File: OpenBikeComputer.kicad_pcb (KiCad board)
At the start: 4 copper layers, 80 x 80 mm, 53 parts, among them J1 USB_C_Receptacle_USB2.0_14P, J2 RJ45_Shielded, J4 Micro_SD_Card_Det1, J5 Conn_01x24_Socket, J6 Conn_01x03_Pin, J7 RFShield_TwoPieces, J8 Conn_01x02_Socket, U1 nRF54L15-QFXX, U2 nPM1300-QEXX, U3 BQ298012RUGR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

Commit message: begin new board
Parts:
- removed J5: Conn_01x24_Socket, Connector_FFC-FPC:TE_2-84952-4_1x24-1MP_P1.0mm_Horizontal
- added J3: Conn_01x30_Socket, Library:CON_541043031_MOL, B.Cu at (172.5, 98.1)
- added SW1: SW_Push, Button_Switch_SMD:SW_SPST_PTS647_Sx50, F.Cu at (157.5, 121.0)
- added SW2: SW_Push, Button_Switch_SMD:SW_SPST_PTS647_Sx50, F.Cu at (167.5, 121.0)
- added SW3: SW_Push, Button_Switch_SMD:SW_SPST_PTS647_Sx50, F.Cu at (177.5, 121.0)
- added SW4: SW_Push, Button_Switch_SMD:SW_SPST_PTS647_Sx50, F.Cu at (187.5, 121.0)
- J1: moved to B.Cu
- J2, J6, R7, R8: moved to F.Cu
- moved J8 67.3 mm to (156.9, 81.5), turned to 90 degrees
- moved U8 66.3 mm to (243.6, 128.9)
- moved D2 61.5 mm to (249.8, 122.8)
- moved L2 61.0 mm to (254.6, 126.8), turned to 0 degrees
- moved R2 61.0 mm to (240.4, 130.2), turned to 0 degrees
- moved D3 60.8 mm to (249.8, 125.8)
- moved D4 60.6 mm to (249.8, 128.9)
- moved C7 60.1 mm to (243.3, 126.2), turned to 0 degrees
- moved R1 59.8 mm to (240.4, 128.2), turned to 0 degrees
- moved C1 59.6 mm to (240.4, 122.3)
- moved C2 58.2 mm to (240.4, 124.2), turned to 0 degrees
- moved C3 57.2 mm to (240.4, 126.2), turned to 0 degrees
- moved U2 57.1 mm to (254.3, 114.9), turned to 0 degrees
- moved L1 56.1 mm to (254.6, 123.1), turned to 0 degrees
- moved C9 55.6 mm to (246.1, 124.2), turned to 0 degrees
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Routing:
- net VDDIO: track 150.7 -> 0.00 mm, vias 9 -> 0
- net SENSE2A: track 54.9 -> 0.00 mm, vias 1 -> 0
- net DETECT1: track 52.8 -> 0.00 mm, vias 1 -> 0
- net SENSE1A: track 52.7 -> 0.00 mm, vias 1 -> 0
- net Net-(J6-Pin_2): track 49.3 -> 0.00 mm, vias 1 -> 0
- net SENSE2B: track 49.3 -> 0.00 mm, vias 1 -> 0
- net Net-(J6-Pin_3): track 48.8 -> 0.00 mm, vias 1 -> 0
- net DETECT2: track 48.6 -> 0.00 mm, vias 1 -> 0
- net SENSE1B: track 47.7 -> 0.00 mm, vias 1 -> 0
- net Net-(AE2-A): track 33.7 -> 0.00 mm
- net SCL1: track 33.1 -> 0.00 mm, vias 2 -> 0
- net VSYS: track 32.3 -> 0.00 mm
- net SDA1: track 31.5 -> 0.00 mm, vias 2 -> 0
- net SD_CS: track 24.1 -> 0.00 mm, vias 2 -> 0
- net SD_MISO: track 24.1 -> 0.00 mm, vias 2 -> 0
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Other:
- board size 80 x 80 mm -> 45 x 60 mm

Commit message: lay out components
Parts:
- removed J2: RJ45_Shielded, Connector_RJ:RJ45_Amphenol_RJHSE538X
- added REF**: NHD-1.91-176176UBC3, Library:NHD-1.91-176176UBC3, F.Cu at (163.2, 85.8)
- J4: moved to B.Cu
- moved J4 87.6 mm to (156.2, 94.4), turned to 90 degrees
- moved J7 50.9 mm to (175.6, 98.7)
- moved AE2 47.1 mm to (189.2, 98.9), turned to -90 degrees
- moved J3 8.40 mm to (172.5, 106.5)
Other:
- outline, holes or cut-outs redrawn

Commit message: housekeeping
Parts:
- moved J6 110.8 mm to (151.6, 103.9)
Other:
- board text removed: "20250126_ly2_s6_w12"
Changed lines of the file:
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@@
 	(footprint "Connector_PinHeader_1.27mm:PinHeader_1x03_P1.27mm_Vertical"
 		(layer "F.Cu")
-		(at 261.5 89.53)
+		(at 151.6 103.86)
 		(descr "Through hole straight pin header, 1x03, 1.27mm pitch, single row")
 		(tags "Through hole pin header THT 1x03 1.27mm single row")
@@
 	)
 	(footprint "RF_Antenna:Texas_SWRA117D_2.4GHz_Right"
+		(locked yes)
 		(layer "F.Cu")
 		(at 189.175 98.9 -90)
@@
 	)
 	(footprint "Library:CON_541043031_MOL"
+		(locked yes)
 		(layer "B.Cu")
 		(at 172.5 106.5 180)
@@
 	)
 	(gr_line
-		(start 6.825 11.821246)
-		(end 20.25115 35.07602)
-		(stroke
-			(width 0.127)
-			(type default)
-		)
-		(layer "F.SilkS")
-	)
-	(gr_line
-		(start 13.65 0)
-		(end 40.5023 0)
-		(stroke
-			(width 0.127)
-			(type default)
-		)
-		(layer "F.SilkS")
-	)
-	(gr_line
-		(start -6.825 -11.821246)
-		(end -20.25115 -35.07602)
-		(stroke
-			(width 0.127)
-			(type default)
-		)
-		(layer "F.SilkS")
-	)
-	(gr_line
-		(start -13.65 0)
-		(end -40.5023 0)
-		(stroke
-			(width 0.127)
-			(type default)
-		)
-		(layer "F.SilkS")
-	)
-	(gr_line
-		(start -6.824999 11.821246)
-		(end -20.251149 35.07602)
-		(stroke
-			(width 0.127)
-			(type default)
-		)
-		(layer "F.SilkS")
-	)
-	(gr_circle
-		(center 0 0)
-		(end 13 0)
-		(stroke
-			(width 0.1)
-			(type default)
-		)
-		(fill none)
-		(layer "F.SilkS")
-	)
-	(gr_circle
-		(center 0 0)
-		(end 42.634 0)
-		(stroke
-			(width 0.1)
-			(type default)
-		)
-		(fill none)
-		(layer "F.SilkS")
-	)
-	(gr_line
-		(start 6.824999 -11.821246)
-		(end 20.251149 -35.07602)
-		(stroke
-			(width 0.127)
-			(type default)
-		)
-		(layer "F.SilkS")
-	)
-	(gr_line
 		(start 195 135)
 		(end 195 75)
@@
 		)
 	)
-	(gr_text "20250126_ly2_s6_w12"
-		(at 0 48.5 0)
-		(layer "F.SilkS")
-		(effects
-			(font
-				(size 0.5 0.5)
-			)
-		)
-	)
 	(zone
 		(net 0)
 		(net_name "")
+		(locked yes)
 		(layers "F.Cu" "In1.Cu" "In2.Cu" "B.Cu")
 		(name "antenna")
@@
 		(polygon
 			(pts
-				(xy 189.4 97.5) (xy 188.5 97.5) (xy 188.5 112.5) (xy 195 112.5) (xy 195 95) (xy 189.4 95)
+				(xy 189.4 99.5) (xy 188.5 99.5) (xy 188.5 112.5) (xy 195 112.5) (xy 195 95) (xy 189.4 95)
 			)
 		)
@@
 			)
 		)
-	)
-	(zone
-		(net 0)
-		(net_name "")
-		(layers "*.Mask")
-		(hatch edge 0.5)
-		(connect_pads
-			(clearance 0)
-		)
-		(min_thickness 0.25)
-		(filled_areas_thickness no)
-		(fill yes
-			(thermal_gap 0.5)
-			(thermal_bridge_width 0.5)
-			(island_removal_mode 1)
-			(island_area_min 10)
-		)
-		(polygon
-			(pts
-				(xy 49.999999 20.710678) (xy 20.710678 49.999999) (xy -20.710678 49.999999) (xy -49.999999 20.710678)
-				(xy -49.999999 -20.710678) (xy -20.710678 -49.999999) (xy 20.710678 -49.999999) (xy 49.999999 -20.710678)
-			)
-		)
-		(polygon
-			(pts
-				(xy 44.999999 18.63961) (xy 18.63961 44.999999) (xy -18.63961 44.999999) (xy -44.999999 18.63961)
-				(xy -44.999999 -18.63961) (xy -18.63961 -44.999999) (xy 18.63961 -44.999999) (xy 44.999999 -18.63961)
-			)
-		)
-	)
-	(zone
-		(net 0)
-		(net_name "")
-		(layers "*.Mask")
-		(hatch edge 0.5)
-		(connect_pads
-			(clearance 0)
-		)
-		(min_thickness 0.25)
-		(filled_areas_thickness no)
-		(fill yes
-			(thermal_gap 0.5)
-			(thermal_bridge_width 0.5)
-			(island_removal_mode 1)
-			(island_area_min 10)
-		)
-		(polygon
-			(pts
-				(xy 11.392 0) (xy 11.36952 0.715309) (xy 11.30217 1.427796) (xy 11.190216 2.134647) (xy 11.034099 2.833075)
-				(xy 10.834435 3.520321) (xy 10.592013 4.193674) (xy 10.307789 4.850477) (xy 9.982885 5.488137) (xy 9.618583 6.104138)
-				(xy 9.216321 6.696049) (xy 8.777686 7.261534) (xy 8.30441 7.79836) (xy 7.79836 8.30441) (xy 7.261534 8.777686)
-				(xy 6.696049 9.216321) (xy 6.104138 9.618583) (xy 5.488137 9.982885) (xy 4.850477 10.307789) (xy 4.193674 10.592013)
-				(xy 3.520321 10.834435) (xy 2.833075 11.034099) (xy 2.134647 11.190216) (xy 1.427796 11.30217) (xy 0.715309 11.36952)
-				(xy 0 11.392) (xy -0.715309 11.36952) (xy -1.427796 11.30217) (xy -2.134647 11.190216) (xy -2.833075 11.034099)
-				(xy -3.520321 10.834435) (xy -4.193674 10.592013) (xy -4.850477 10.307789) (xy -5.488137 9.982885)
-				(xy -6.104138 9.618583) (xy -6.696049 9.216321) (xy -7.261534 8.777686) (xy -7.79836 8.30441) (xy -8.30441 7.79836)
-				(xy -8.777686 7.261534) (xy -9.216321 6.696049) (xy -9.618583 6.104138) (xy -9.982885 5.488137)
-				(xy -10.307789 4.850477) (xy -10.592013 4.193674) (xy -10.834435 3.520321) (xy -11.034099 2.833075)
-				(xy -11.190216 2.134647) (xy -11.30217 1.427796) (xy -11.36952 0.715309) (xy -11.392 0) (xy -11.36952 -0.715309)
-				(xy -11.30217 -1.427796) (xy -11.190216 -2.134647) (xy -11.034099 -2.833075) (xy -10.834435 -3.520321)
-				(xy -10.592013 -4.193674) (xy -10.307789 -4.850477) (xy -9.982885 -5.488137) (xy -9.618583 -6.104138)
-				(xy -9.216321 -6.696049) (xy -8.777686 -7.261534) (xy -8.30441 -7.79836) (xy -7.79836 -8.30441)
-				(xy -7.261534 -8.777686) (xy -6.696049 -9.216321) (xy -6.104138 -9.618583) (xy -5.488137 -9.982885)
-				(xy -4.850477 -10.307789) (xy -4.193674 -10.592013) (xy -3.520321 -10.834435) (xy -2.833075 -11.034099)
-				(xy -2.134647 -11.190216) (xy -1.427796 -11.30217) (xy -0.715309 -11.36952) (xy 0 -11.392) (xy 0.715309 -11.36952)
-				(xy 1.427796 -11.30217) (xy 2.134647 -11.190216) (xy 2.833075 -11.034099) (xy 3.520321 -10.834435)
-				(xy 4.193674 -10.592013) (xy 4.850477 -10.307789) (xy 5.488137 -9.982885) (xy 6.104138 -9.618583)
-				(xy 6.696049 -9.216321) (xy 7.261534 -8.777686) (xy 7.79836 -8.30441) (xy 8.30441 -7.79836) (xy 8.777686 -7.261534)
-				(xy 9.216321 -6.696049) (xy 9.618583 -6.104138) (xy 9.982885 -5.488137) (xy 10.307789 -4.850477)
-				(xy 10.592013 -4.193674) (xy 10.834435 -3.520321) (xy 11.034099 -2.833075) (xy 11.190216 -2.134647)
-				(xy 11.30217 -1.427796) (xy 11.36952 -0.715309)
-			)
-		)

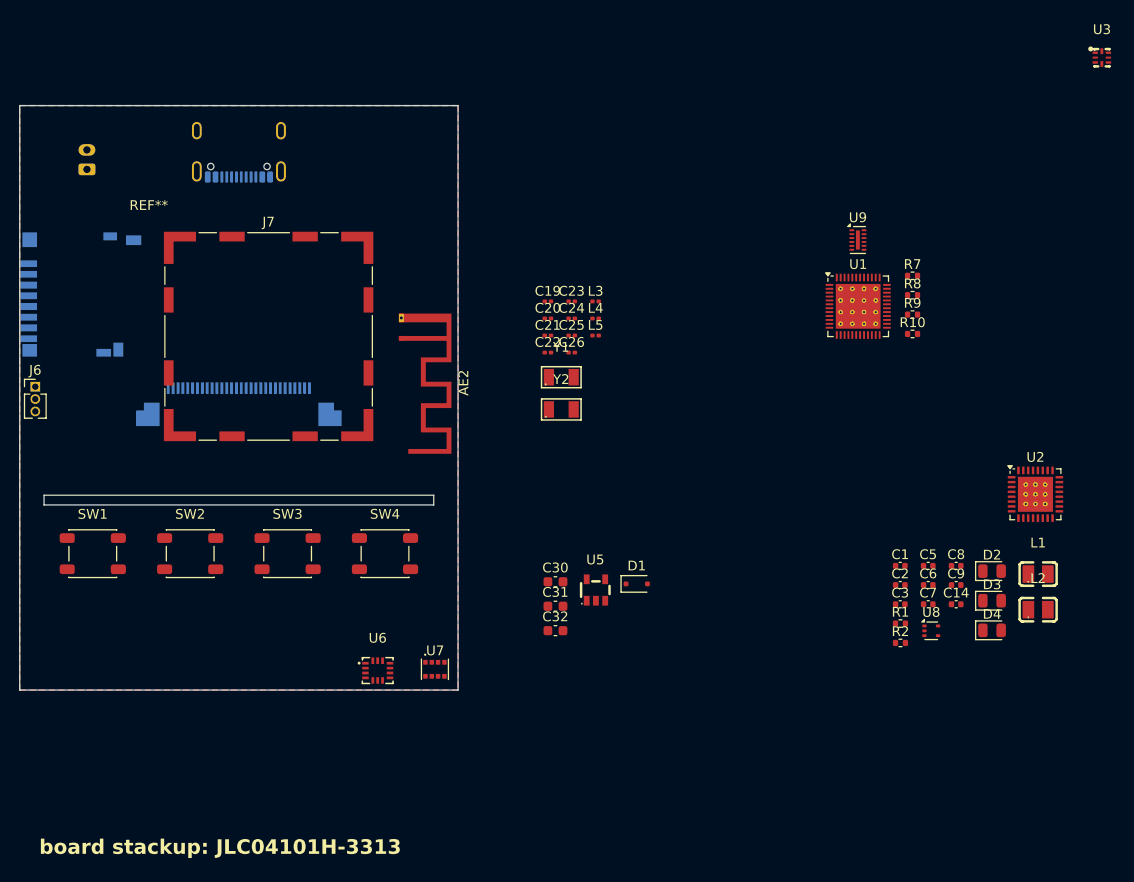
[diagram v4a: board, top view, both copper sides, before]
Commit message: route PMIC
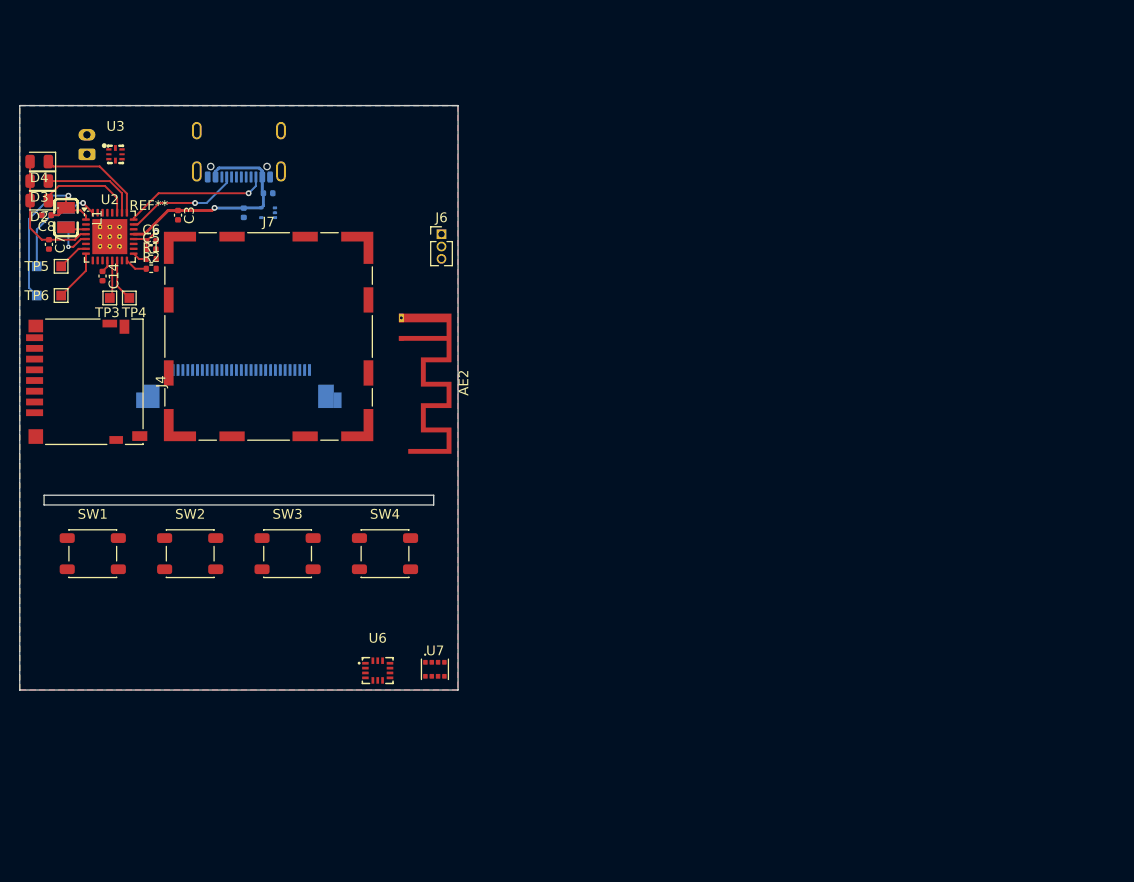
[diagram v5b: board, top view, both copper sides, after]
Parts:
- removed C19: 1.5pF, Capacitor_SMD:C_0201_0603Metric
- removed C20: 2.0pF, Capacitor_SMD:C_0201_0603Metric
- removed C21: 0.3pF, Capacitor_SMD:C_0201_0603Metric
- removed C22: 10uF, Capacitor_SMD:C_0201_0603Metric
- removed C23, C24, C25, C26: 100nF, Capacitor_SMD:C_0201_0603Metric
- removed C30, C32: 4.7uF, Capacitor_SMD:C_0603_1608Metric
- removed C31: 120pF, Capacitor_SMD:C_0603_1608Metric
- removed D1: BAT54J, Diode_SMD:D_SOD-323F
- removed L3: 2.7nH, Inductor_SMD:L_0201_0603Metric
- removed L4, L5: 3.5nH, Inductor_SMD:L_0201_0603Metric
- removed R10, R7, R8, R9: 10k, Resistor_SMD:R_0402_1005Metric
- removed U1: nRF54L15-QFXX, Package_DFN_QFN:QFN-48-1EP_6x6mm_P0.4mm_EP4.6x4.6mm_ThermalVias
- removed U5: FAN5331SX, Library:SOT-23-5_L2.9-W1.6-P0.95-LS2.8-BL
- removed U9: TPD6F003, Package_SON:Texas_R-PWSON-N12_EP0.4x2mm
- removed Y1: 32MHz, Library:CRYSTAL-SMD_L3.2-W1.5-1
- removed Y2: 32.768KHz, Library:CRYSTAL-SMD_L3.2-W1.5-1
- added TP1: TestPoint, TestPoint:TestPoint_Pad_1.0x1.0mm, B.Cu at (151.8, 94.5)
- added TP2: TestPoint, TestPoint:TestPoint_Pad_1.0x1.0mm, B.Cu at (151.8, 91.5)
- added TP3: TestPoint, TestPoint:TestPoint_Pad_1.0x1.0mm, F.Cu at (159.2, 94.8)
- added TP4: TestPoint, TestPoint:TestPoint_Pad_1.0x1.0mm, F.Cu at (161.2, 94.8)
- added TP5: TestPoint, TestPoint:TestPoint_Pad_1.0x1.0mm, F.Cu at (154.2, 91.5)
- added TP6: TestPoint, TestPoint:TestPoint_Pad_1.0x1.0mm, F.Cu at (154.2, 94.5)
- C1, C2, C9, L2, U8: moved to B.Cu
- J4: moved to F.Cu
- moved D4 109.0 mm to (152.0, 80.8), turned to 180 degrees
- moved L2 107.6 mm to (154.8, 86.5), turned to -90 degrees
- moved D3 106.9 mm to (152.0, 82.8), turned to 180 degrees
- moved L1 106.3 mm to (154.8, 86.5), turned to -90 degrees
- moved D2 105.0 mm to (152.0, 84.8), turned to 180 degrees
- moved U3 101.8 mm to (159.8, 80.0)
- moved C9 100.8 mm to (152.8, 86.2), turned to 180 degrees
- moved C8 100.1 mm to (152.8, 86.2), turned to 180 degrees
- moved U2 98.6 mm to (159.2, 88.5)
- moved C7 97.5 mm to (153.0, 89.2), turned to -90 degrees
- moved C14 93.9 mm to (158.5, 92.5), turned to -90 degrees
- moved C6 87.2 mm to (163.5, 88.9)
- moved C5 86.1 mm to (163.5, 89.8)
- moved R2 86.0 mm to (163.5, 91.8)
- moved R1 85.5 mm to (163.5, 90.8)
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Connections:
- net /Battery/VBATOUT renamed +BATT
- net VBUSIN renamed VBUS
- C14 pad 1: VDDIO -> +1V8
- C8 pad 1: VDDIO -> +1V8
- C9 pad 1: /Display/3.0V -> +3V0
- J4 pad 4: VDDIO -> +3V0
- L1 pad 1: VDDIO -> +1V8
- L2 pad 1: /Display/3.0V -> +3V0
- U2 pad 1: VDDIO -> +1V8
- U2 pad 12: VDDIO -> +1V8
- U2 pad 32: /Display/3.0V -> +3V0
- U6 pad 5: VDDIO -> +1V8
- U6 pad 8: VDDIO -> +1V8
- U7 pad 8: VDDIO -> +1V8
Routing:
- net VBUS: track 0.00 -> 23.9 mm, vias 0 -> 1
- net +1V8: track 0.00 -> 21.0 mm, vias 0 -> 1
- net VSYS: track 0.00 -> 16.9 mm, vias 0 -> 1
- net CC2: track 0.00 -> 15.0 mm, vias 0 -> 1
- net CC1: track 0.00 -> 11.9 mm, vias 0 -> 1
- net Net-(D4-K): track 0.00 -> 11.4 mm
- net +3V0: track 0.00 -> 11.1 mm, vias 0 -> 1
- net Net-(D3-K): track 0.00 -> 10.1 mm
- net Net-(D2-K): track 0.00 -> 9.96 mm
- net /MCU/INT: track 0.00 -> 5.36 mm
- net SCL1: track 0.00 -> 4.37 mm
- net Net-(U2-SW2): track 0.00 -> 4.23 mm, vias 0 -> 1
- net SDA1: track 0.00 -> 3.95 mm
- net /MCU/RESET: track 0.00 -> 3.30 mm
- net Net-(U2-VSET2): track 0.00 -> 2.34 mm
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
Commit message: start routing MCU + switch out pin assignments
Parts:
- added C19: 1.5pF, Capacitor_SMD:C_0201_0603Metric, F.Cu at (180.5, 98.2)
- added C20: 2.0pF, Capacitor_SMD:C_0201_0603Metric, F.Cu at (181.9, 98.2)
- added C21: 0.3pF, Capacitor_SMD:C_0201_0603Metric, F.Cu at (183.3, 98.2)
- added L3: 2.7nH, Inductor_SMD:L_0201_0603Metric, F.Cu at (180.5, 98.9)
- added L4: 3.5nH, Inductor_SMD:L_0201_0603Metric, F.Cu at (181.9, 98.9)
- added L5: 3.5nH, Inductor_SMD:L_0201_0603Metric, F.Cu at (183.3, 98.9)
- added R7: 10k, Resistor_SMD:R_0402_1005Metric, F.Cu at (177.5, 92.2)
- added R8: 10k, Resistor_SMD:R_0402_1005Metric, F.Cu at (179.0, 92.2)
- added U1: nRF54L15-QFXX, Package_DFN_QFN:QFN-48-1EP_6x6mm_P0.4mm_EP4.6x4.6mm_ThermalVias, F.Cu at (176.1, 99.0)
- moved U3 1.90 mm to (161.2, 78.8)
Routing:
- net SDA1: track 3.95 -> 28.4 mm, vias 0 -> 2
- net SCL1: track 4.37 -> 25.1 mm, vias 0 -> 2
- net Net-(AE2-A): track 0.00 -> 6.26 mm
- net Net-(C19-Pad1): track 0.00 -> 1.46 mm
- net Net-(C20-Pad1): track 0.00 -> 1.46 mm
- net GND: track 0.00 -> 1.28 mm
- net Net-(U1-ANT): track 0.00 -> 1.20 mm

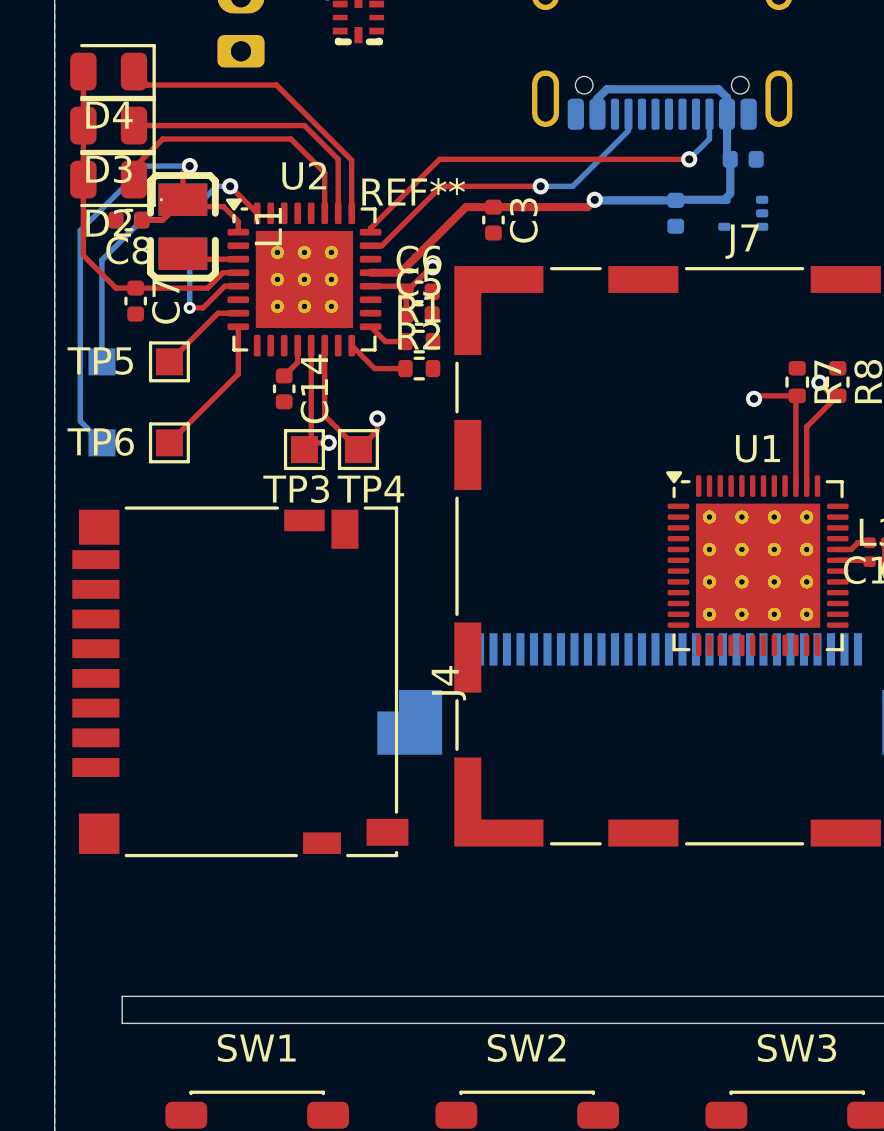
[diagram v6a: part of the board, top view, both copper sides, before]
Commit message: sd card (todo see if we can use a better connector to avoid routing like this)
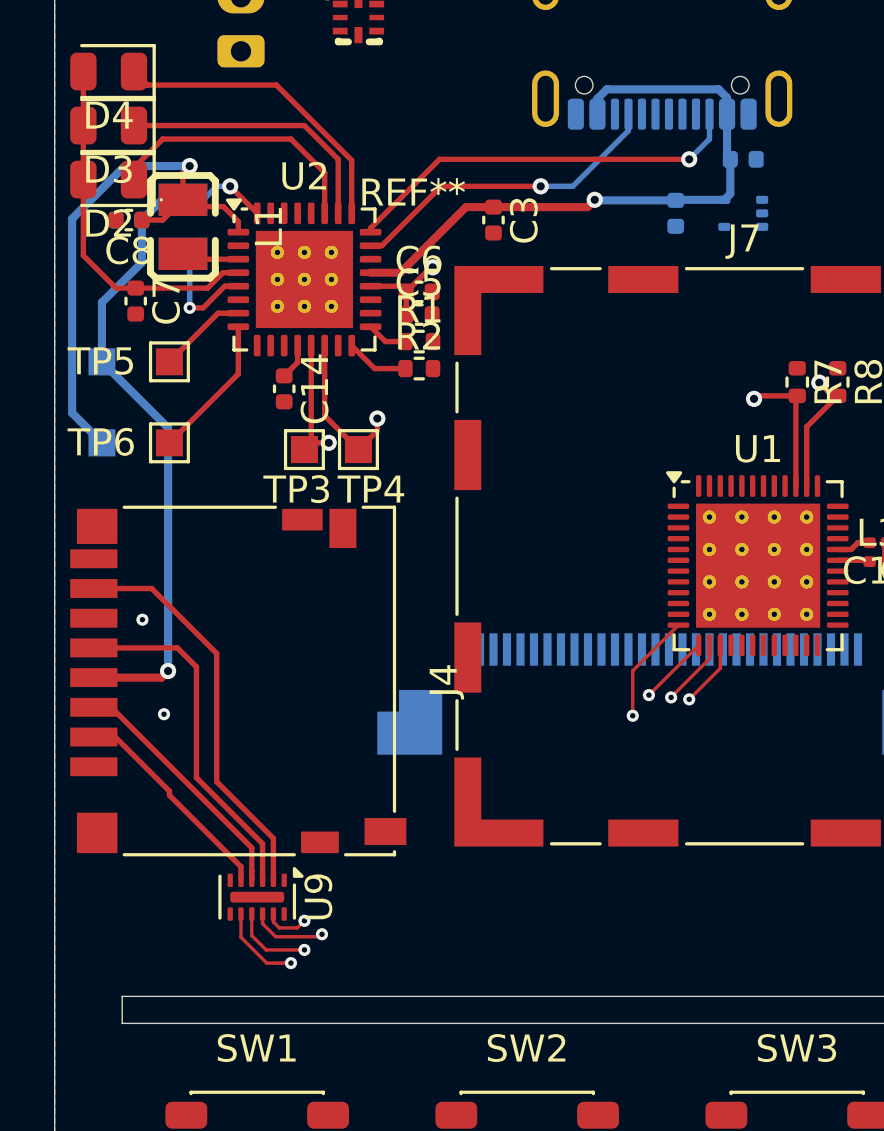
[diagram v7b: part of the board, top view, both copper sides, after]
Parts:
- added U9: TPD6F003, Package_SON:Texas_R-PWSON-N12_EP0.4x2mm, F.Cu at (157.5, 111.3)
- moved J4 0.08 mm to (156.8, 103.3)
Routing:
- net SD_CS: track 0.00 -> 24.4 mm, vias 0 -> 2
- net SD_MOSI: track 0.00 -> 22.9 mm, vias 0 -> 2
- net SD_SCLK: track 0.00 -> 21.7 mm, vias 0 -> 2
- net SD_MISO: track 0.00 -> 20.6 mm, vias 0 -> 2
- net +3V0: track 11.1 -> 26.4 mm, vias 1 -> 2
- net Net-(J4-DAT0): track 0.00 -> 14.8 mm
- net Net-(J4-CLK): track 0.00 -> 13.0 mm
- net Net-(J4-CMD): track 0.00 -> 9.21 mm
- net Net-(J4-DAT3/CD): track 0.00 -> 8.03 mm
- net +1V8: track 21.0 -> 21.6 mm
- net GND: vias 0 -> 2
